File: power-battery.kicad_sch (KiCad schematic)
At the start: 6 parts, among them J2 S2B-PH-K-SLFSN, U5 MCP73831-2-OT

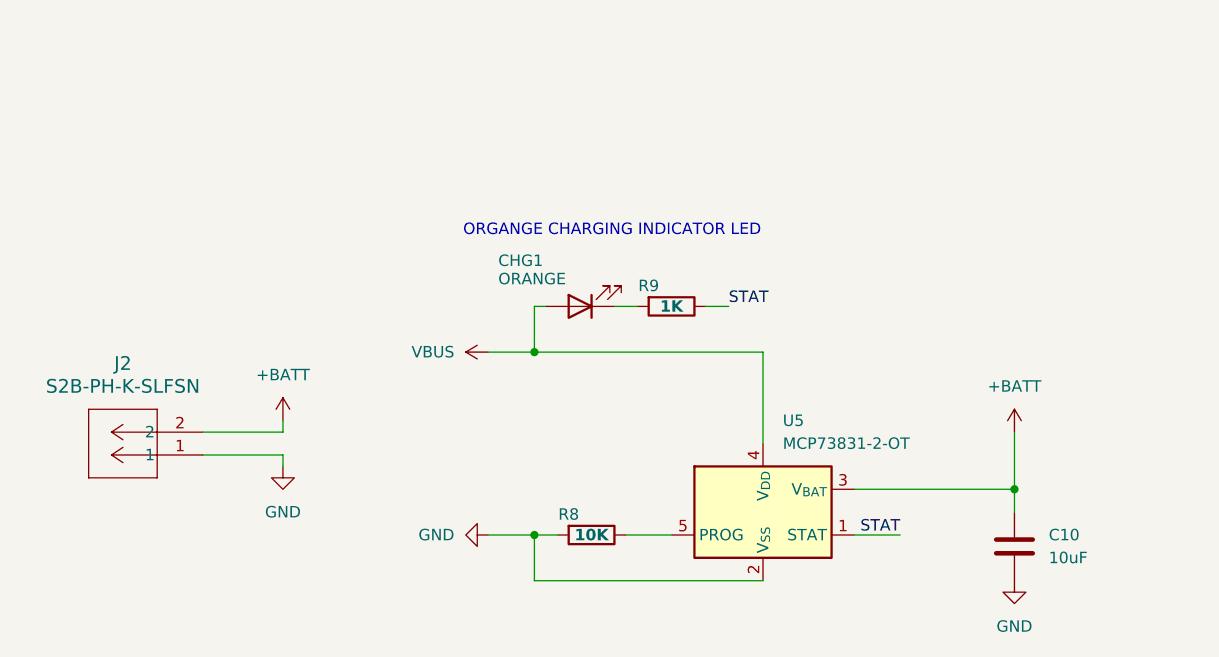
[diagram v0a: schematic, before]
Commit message: Adding symbols information
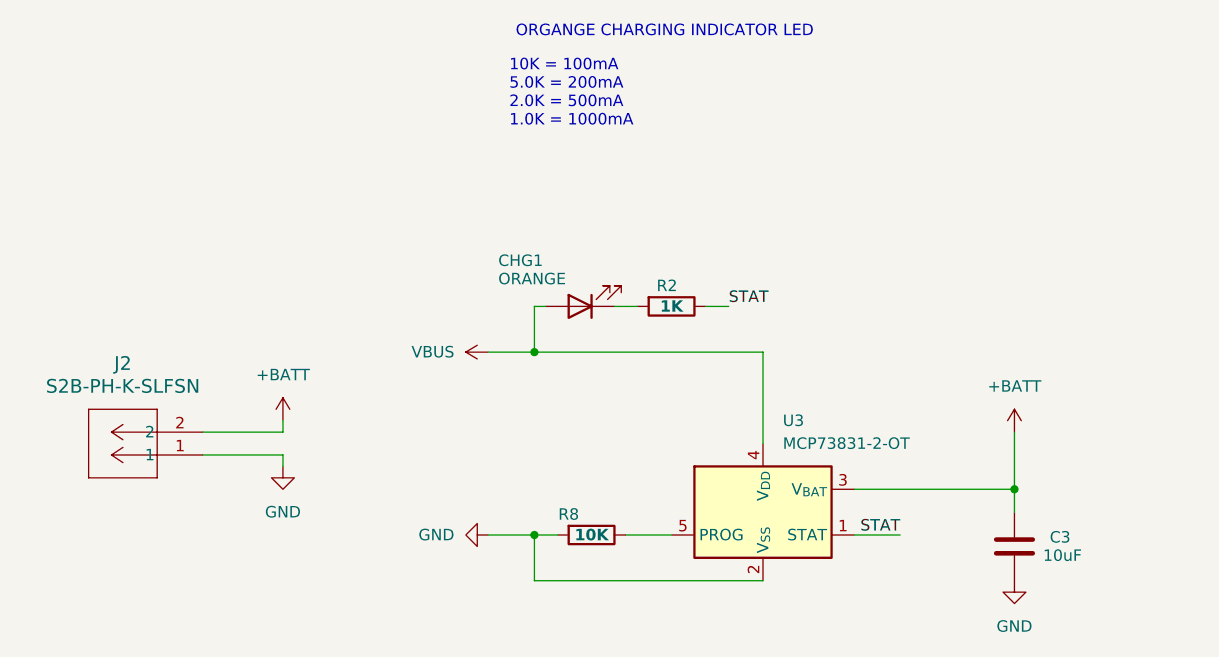
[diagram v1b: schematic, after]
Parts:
- removed C10: 10uF, symbol Device:C
- added C3: 10uF, Inductor_SMD:L_0805_2012Metric, symbol Device:C
- CHG1: footprint (none) -> LED_SMD:LED_0805_2012Metric; Mfr (none) -> Harvatek Corporation; Mfr P/N (none) -> B1701UD--20D000414U1930; Supplier_1 (none) -> Digikey; Supplier_1 P/N (none) -> 3147-B1701UD--20D000414U1930CT-ND; Supplier_1 Price @ Qty (none) -> 0.092; Supplier_1 Unit Price (none) -> 0.10
- R2: renamed from R9; footprint (none) -> Capacitor_SMD:C_0603_1608Metric; Mfr (none) -> Vishay Beyschlag/Draloric/BC Components; Mfr P/N (none) -> MCT06030C1001FP500; Supplier_1 (none) -> Digikey; Supplier_1 P/N (none) -> MCT0603-1.00K-CFCT-ND; Supplier_1 Price @ Qty (none) -> 0.02280; Supplier_1 Unit Price (none) -> 0.10
- U3: renamed from U5; Mfr (none) -> Microchip Technology; Mfr P/N (none) -> MCP73831T-2ATI/OT; Supplier_1 (none) -> Digikey; Supplier_1 P/N (none) -> MCP73831T-2AT|/OTCT-ND; Supplier_1 Price @ Qty (none) -> 0.6125; Supplier_1 Unit Price (none) -> 0.76
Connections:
- net +BATT: now also C3.1
- net GND: now also C3.2
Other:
- note added: "10K = 100mA 5.0K = 200mA 2.0K = 500mA 1.0K = 1000mA"
- company: (none) -> catbranchman
- title: (none) -> Power - Battery Charing

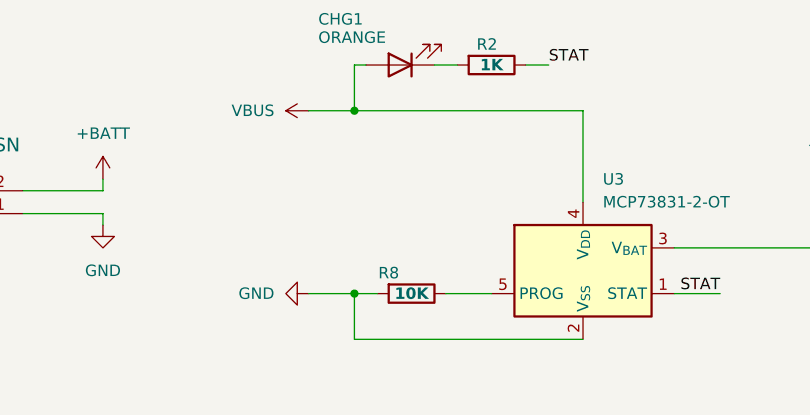
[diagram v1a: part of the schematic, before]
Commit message: Fixing footprint imports
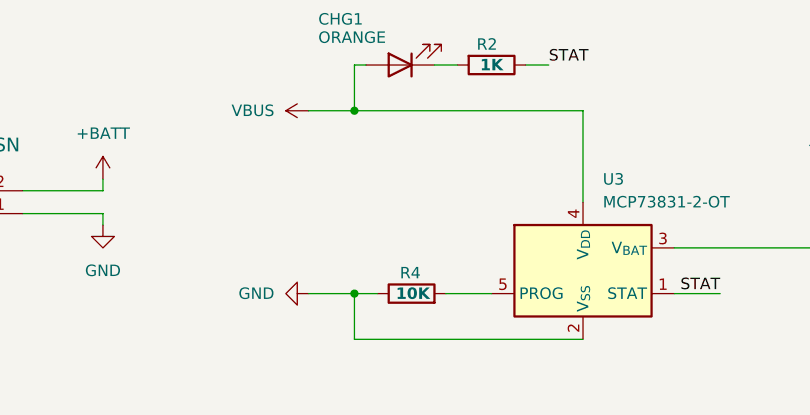
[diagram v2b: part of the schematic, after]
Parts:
- removed R8: 10K, symbol Device:R
- added R4: 10K, Resistor_SMD:R_0603_1608Metric, symbol Device:R
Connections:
- net GND: now also R4.1
- net at U3.5 (PROG): now also R4.2
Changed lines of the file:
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@@
-	)
-	(symbol
-		(lib_id "Device:R")
-		(at 146.05 109.22 270)
-		(unit 1)
-		(exclude_from_sim no)
-		(in_bom yes)
-		(on_board yes)
-		(dnp no)
-		(property "Reference" "R8"
-			(at 143.51 106.934 90)
-			(effects
-				(font
-					(size 1.27 1.27)
-				)
-			)
-		)
-		(property "Value" "10K"
-			(at 146.05 109.22 90)
-			(effects
-				(font
-					(size 1.27 1.27)
-					(thickness 0.254)
-					(bold yes)
-				)
-			)
-		)
-		(property "Footprint" ""
-			(at 146.05 107.442 90)
-			(effects
-				(font
-					(size 1.27 1.27)
-				)
-				(hide yes)
-			)
-		)
-		(property "Datasheet" "~"
-			(at 146.05 109.22 0)
-			(effects
-				(font
-					(size 1.27 1.27)
-				)
-				(hide yes)
-			)
-		)
-		(property "Description" "Resistor"
-			(at 146.05 109.22 0)
-			(effects
-				(font
-					(size 1.27 1.27)
-				)
-				(hide yes)
-			)
-		)
-		(pin "2"
-		)
-		(pin "1"
-		)
-		(instances
-			(project "roamer"
-				(path "/1c59de6a-87fe-4223-8898-4b0383164a31/8b882434-0721-40fe-a26c-3dd045b3f675"
-					(reference "R8")
-					(unit 1)
-				)
-			)
-		)
 	)
 	(symbol
@@
 					(unit 1)
 				)
+			)
+		)
+	)
+	(symbol
+		(lib_id "Device:R")
+		(at 146.05 109.22 90)
+		(unit 1)
+		(exclude_from_sim no)
+		(in_bom yes)
+		(on_board yes)
+		(dnp no)
+		(property "Reference" "R4"
+			(at 147.066 106.934 90)
+			(effects
+				(font
+					(size 1.27 1.27)
+				)
+				(justify left)
+			)
+		)
+		(property "Value" "10K"
+			(at 148.082 109.22 90)
+			(effects
+				(font
+					(size 1.27 1.27)
+					(thickness 0.254)
+					(bold yes)
+				)
+				(justify left)
+			)
+		)
+		(property "Footprint" "Resistor_SMD:R_0603_1608Metric"
+			(at 146.05 110.998 90)
+			(effects
+				(font
+					(size 1.27 1.27)
+				)
+				(hide yes)
+			)
+		)
+		(property "Datasheet" "https://www.seielect.com/catalog/sei-rncp.pdf"
+			(at 146.05 109.22 0)
+			(effects
+				(font
+					(size 1.27 1.27)
+				)
+				(hide yes)
+			)
+		)
+		(property "Description" "10 kOhms 1% 0.125W, 1/8W Chip Resistor 0603 (1608 Metric) Anti-Sulfur Thin Film"
+			(at 146.05 109.22 0)
+			(effects
+				(font
+					(size 1.27 1.27)
+				)
+				(hide yes)
+			)
+		)
+		(property "Mfr" "Stackpole Electronics Inc"
+			(at 146.05 109.22 0)
+			(effects
+				(font
+					(size 1.27 1.27)
+				)
+				(hide yes)
+			)
+		)
+		(property "Mfr P/N" "RNCP0603FTD10K0"
+			(at 146.05 109.22 0)
+			(effects
+				(font
+					(size 1.27 1.27)
+				)
+				(hide yes)
+			)
+		)
+		(property "Supplier_1" "Digikey"
+			(at 146.05 109.22 0)
+			(effects
+				(font
+					(size 1.27 1.27)
+				)
+				(hide yes)
+			)
+		)
+		(property "Supplier_1 P/N" "RNCP0603FTD10K0CT-ND"
+			(at 146.05 109.22 0)
+			(effects
+				(font
+					(size 1.27 1.27)
+				)
+				(hide yes)
+			)
+		)
+		(property "Supplier_1 Unit Price" "0.10"
+			(at 146.05 109.22 0)
+			(effects
+				(font
+					(size 1.27 1.27)
+				)
+				(hide yes)
+			)
+		)
+		(property "Supplier_1 Price @ Qty" "0.0170"
+			(at 146.05 109.22 0)
+			(effects
+				(font
+					(size 1.27 1.27)
+				)
+				(hide yes)
+			)
+		)
+		(property "Supplier_2" ""
+			(at 146.05 109.22 0)
+			(effects
+				(font
+					(size 1.27 1.27)
+				)
+				(hide yes)
+			)
+		)
+		(property "Supplier_2 P/N" ""
+			(at 146.05 109.22 0)
+			(effects
+				(font
+					(size 1.27 1.27)
+				)
+				(hide yes)
+			)
+		)
+		(property "Supplier_2 Unit Price" ""
+			(at 146.05 109.22 0)
+			(effects
+				(font
+					(size 1.27 1.27)
+				)
+				(hide yes)
+			)
+		)
+		(property "Supplier_2 Price @ Qty" ""
+			(at 146.05 109.22 0)
+			(effects
+				(font
+					(size 1.27 1.27)
+				)
+				(hide yes)
+			)
+		)
+		(pin "2"
+		)
+		(pin "1"
+		)
+		(instances
+			(project "roamer"
+				(path "/1c59de6a-87fe-4223-8898-4b0383164a31/8b882434-0721-40fe-a26c-3dd045b3f675"
+					(reference "R4")
+					(unit 1)
+				)

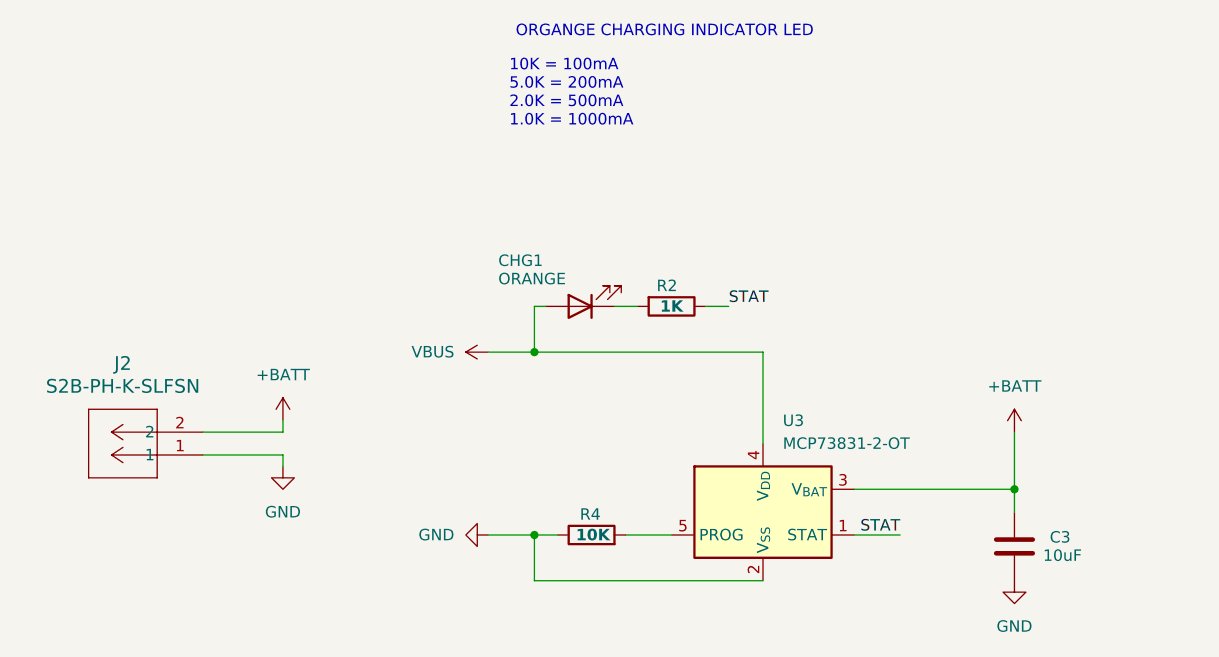
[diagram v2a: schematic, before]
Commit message: Adding more 0 ohm resistors and pullups for I2C lines
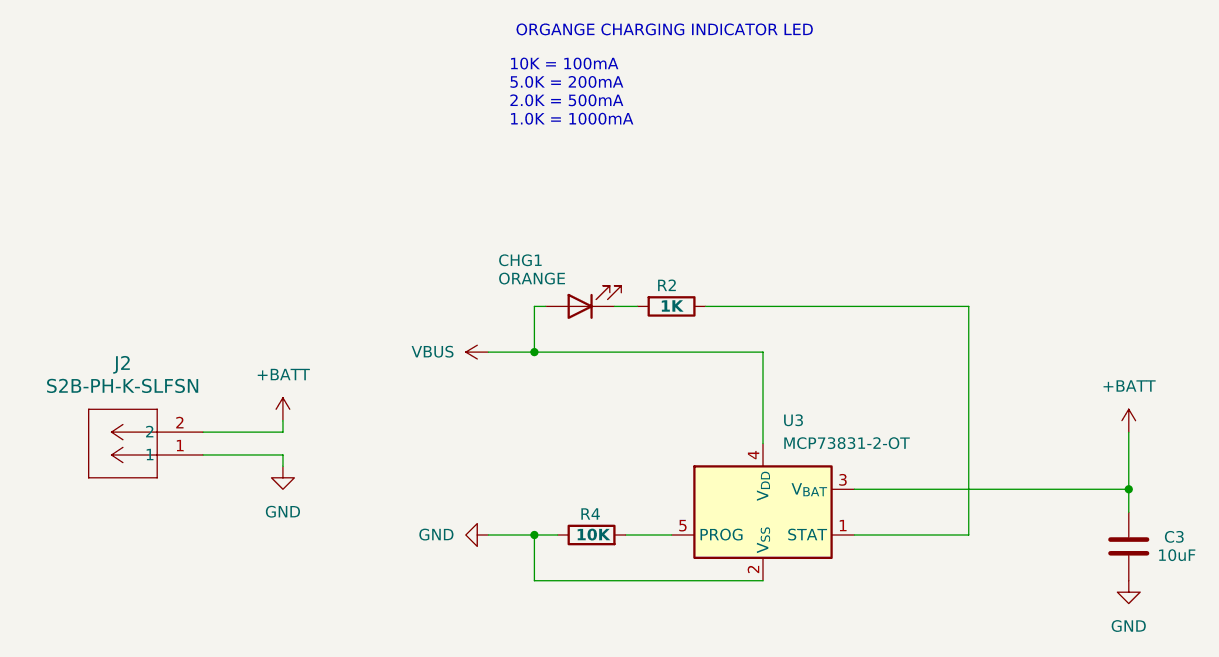
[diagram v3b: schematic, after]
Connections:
- net STAT: no longer names the net of R2.1, U3.1 (STAT)
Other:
- moved on the sheet: C3
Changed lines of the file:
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@@
 	)
 	(junction
-		(at 193.04 104.14)
+		(at 205.74 104.14)
 		(diameter 0)
 		(color 0 0 0 0)
@@
 	(wire
 		(pts
-			(xy 193.04 106.68) (xy 193.04 104.14)
+			(xy 205.74 106.68) (xy 205.74 104.14)
 		)
 		(stroke
@@
 	(wire
 		(pts
-			(xy 158.75 83.82) (xy 161.29 83.82)
+			(xy 158.75 83.82) (xy 187.96 83.82)
 		)
 		(stroke
@@
 	(wire
 		(pts
-			(xy 193.04 97.79) (xy 193.04 104.14)
-		)
-		(stroke
-			(width 0)
-			(type default)
-		)
-	)
-	(wire
-		(pts
-			(xy 175.26 104.14) (xy 193.04 104.14)
-		)
-		(stroke
-			(width 0)
-			(type default)
-		)
-	)
-	(wire
-		(pts
-			(xy 180.34 109.22) (xy 175.26 109.22)
+			(xy 205.74 97.79) (xy 205.74 104.14)
+		)
+		(stroke
+			(width 0)
+			(type default)
+		)
+	)
+	(wire
+		(pts
+			(xy 175.26 104.14) (xy 205.74 104.14)
+		)
+		(stroke
+			(width 0)
+			(type default)
+		)
+	)
+	(wire
+		(pts
+			(xy 175.26 109.22) (xy 187.96 109.22)
 		)
 		(stroke
@@
 		(pts
 			(xy 139.7 88.9) (xy 165.1 88.9)
+		)
+		(stroke
+			(width 0)
+			(type default)
+		)
+	)
+	(wire
+		(pts
+			(xy 187.96 109.22) (xy 187.96 83.82)
 		)
 		(stroke
@@
 				(size 1.27 1.27)
 			)
-		)
-	)
-	(label "STAT"
-		(at 180.34 109.22 180)
-		(fields_autoplaced yes)
-		(effects
-			(font
-				(size 1.27 1.27)
-			)
-			(justify right bottom)
-		)
-	)
-	(label "STAT"
-		(at 161.29 83.82 0)
-		(fields_autoplaced yes)
-		(effects
-			(font
-				(size 1.27 1.27)
-			)
-			(justify left bottom)
 		)
 	)
@@
 	(symbol
 		(lib_id "Device:C")
-		(at 193.04 110.49 0)
+		(at 205.74 110.49 0)
 		(unit 1)
 		(exclude_from_sim no)
@@
 		(dnp no)
 		(property "Reference" "C3"
-			(at 198.12 109.474 0)
+			(at 210.82 109.474 0)
 			(effects
 				(font
@@
 		)
 		(property "Value" "10uF"
-			(at 198.374 111.506 0)
+			(at 211.074 111.506 0)
 			(effects
 				(font
@@
 		)
 		(property "Footprint" "Inductor_SMD:L_0805_2012Metric"
-			(at 194.0052 114.3 0)
+			(at 206.7052 114.3 0)
 			(effects
 				(font
@@
 		)
 		(property "Datasheet" "https://mm.digikey.com/Volume0/opasdata/d220001/medias/docus/609/CL21A106K0QNNNE_Sp"
-			(at 193.04 110.49 0)
+			(at 205.74 110.49 0)
 			(effects
 				(font
@@
 		)
 		(property "Description" "10 uF 10% 16V Ceramic Capacitor X5R 0805 (2012 Metric)"
-			(at 193.04 110.49 0)
+			(at 205.74 110.49 0)
 			(effects
 				(font
@@
 		)
 		(property "Mfr" "Samsung Electro-Mechanics"
-			(at 193.04 110.49 0)
+			(at 205.74 110.49 0)
 			(effects
 				(font
@@
 		)
 		(property "Mfr P/N" "CL21A106KOQNNNE"
-			(at 193.04 110.49 0)
+			(at 205.74 110.49 0)
 			(effects
 				(font
@@
 		)
 		(property "Supplier_1" "Digikey"
-			(at 193.04 110.49 0)
+			(at 205.74 110.49 0)
 			(effects
 				(font
@@
 		)
 		(property "Supplier_1 P/N" "1276-1096-1-ND"
-			(at 193.04 110.49 0)
+			(at 205.74 110.49 0)
 			(effects
 				(font
@@
 		)
 		(property "Supplier_1 Unit Price" "0.10"
-			(at 193.04 110.49 0)
+			(at 205.74 110.49 0)
 			(effects
 				(font
@@
 		)
 		(property "Supplier_1 Price @ Qty" "0.03130"
-			(at 193.04 110.49 0)
+			(at 205.74 110.49 0)
 			(effects
 				(font
@@
 		)
 		(property "Supplier_2" ""
-			(at 193.04 110.49 0)
+			(at 205.74 110.49 0)
 			(effects
 				(font
@@
 		)
 		(property "Supplier_2 P/N" ""
-			(at 193.04 110.49 0)
+			(at 205.74 110.49 0)
 			(effects
 				(font
@@
 		)
 		(property "Supplier_2 Unit Price" ""
-			(at 193.04 110.49 0)
+			(at 205.74 110.49 0)
 			(effects
 				(font
@@
 		)
 		(property "Supplier_2 Price @ Qty" ""
-			(at 193.04 110.49 0)
+			(at 205.74 110.49 0)
 			(effects
 				(font
@@
 	(symbol
 		(lib_id "power:+BATT")
-		(at 193.04 97.79 0)
+		(at 205.74 97.79 0)
 		(unit 1)
 		(exclude_from_sim no)
@@
 		(fields_autoplaced yes)
 		(property "Reference" "#PWR031"
-			(at 193.04 101.6 0)
+			(at 205.74 101.6 0)
 			(effects
 				(font
@@
 		)
 		(property "Value" "+BATT"
-			(at 193.04 92.71 0)
+			(at 205.74 92.71 0)
 			(effects
 				(font
@@
 		)
 		(property "Footprint" ""
-			(at 193.04 97.79 0)
+			(at 205.74 97.79 0)
 			(effects
 				(font
@@
 		)
 		(property "Datasheet" ""
-			(at 193.04 97.79 0)
+			(at 205.74 97.79 0)
 			(effects
 				(font
@@
 		)
 		(property "Description" "Power symbol creates a global label with name \"+BATT\""
-			(at 193.04 97.79 0)
+			(at 205.74 97.79 0)
 			(effects
 				(font
@@
 	(symbol
 		(lib_id "power:GND")
-		(at 193.04 114.3 0)
+		(at 205.74 114.3 0)
 		(unit 1)
 		(exclude_from_sim no)
@@
 		(fields_autoplaced yes)
 		(property "Reference" "#PWR032"
-			(at 193.04 120.65 0)
+			(at 205.74 120.65 0)
 			(effects
 				(font
@@
 		)
 		(property "Value" "GND"
-			(at 193.04 119.38 0)
+			(at 205.74 119.38 0)
 			(effects
 				(font
@@
 		)
 		(property "Footprint" ""
-			(at 193.04 114.3 0)
+			(at 205.74 114.3 0)
 			(effects
 				(font
@@
 		)
 		(property "Datasheet" ""
-			(at 193.04 114.3 0)
+			(at 205.74 114.3 0)
 			(effects
 				(font
@@
 		)
 		(property "Description" "Power symbol creates a global label with name \"GND\" , ground"
-			(at 193.04 114.3 0)
-			(effects
-				(font
+			(at 205.74 114.3 0)
+			(effects
+				(font

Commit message: Working on layout
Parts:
- J2: value S2B-PH-K-SLFSN -> JSTPH; footprint CONN_S2B-PH-K-S_JST -> Connector_JST:JST_PH_S2B-PH-SM4-TB_1x02-1MP_P2.00mm_Horizontal; Mfr (none) -> JST Sales America Inc.; Mfr P/N (none) -> S2B-PH-SM4-TB; Supplier_1 (none) -> Digikey; Supplier_1 P/N (none) -> 455-S2B-PH-SM4-TBCT-ND; Supplier_1 Price @ Qty (none) -> 0.4143; Supplier_1 Unit Price (none) -> 0.58
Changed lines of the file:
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@@
 	(wire
 		(pts
-			(xy 111.76 97.79) (xy 102.87 97.79)
+			(xy 102.87 97.79) (xy 111.76 97.79)
 		)
 		(stroke
@@
 			)
 		)
-		(property "Value" "S2B-PH-K-SLFSN"
+		(property "Value" "JSTPH"
 			(at 93.98 92.71 0)
 			(effects
@@
 			)
 		)
-		(property "Footprint" "CONN_S2B-PH-K-S_JST"
+		(property "Footprint" "Connector_JST:JST_PH_S2B-PH-SM4-TB_1x02-1MP_P2.00mm_Horizontal"
 			(at 102.87 100.33 0)
 			(effects
@@
 			)
 		)
-		(property "Datasheet" "S2B-PH-K-SLFSN"
+		(property "Datasheet" "https://www.jst-mfg.com/product/pdf/eng/ePH.pdf"
 			(at 102.87 100.33 0)
 			(effects
@@
 			)
 		)
-		(property "Description" ""
-			(at 102.87 100.33 0)
-			(effects
+		(property "Description" "Connector Header Surface Mount, Right Angle 2 position 0.079\" (2.00mm)"
+			(at 102.87 100.33 0)
+			(effects
+				(font
+					(size 1.27 1.27)
+				)
+				(hide yes)
+			)
+		)
+		(property "Mfr" "JST Sales America Inc."
+			(at 102.87 100.33 0)
+			(effects
+				(font
+					(size 1.27 1.27)
+				)
+				(hide yes)
+			)
+		)
+		(property "Mfr P/N" "S2B-PH-SM4-TB"
+			(at 102.87 100.33 0)
+			(effects
+				(font
+					(size 1.27 1.27)
+				)
+				(hide yes)
+			)
+		)
+		(property "Supplier_1" "Digikey"
+			(at 102.87 100.33 0)
+			(effects
+				(font
+					(size 1.27 1.27)
+				)
+				(hide yes)
+			)
+		)
+		(property "Supplier_1 P/N" "455-S2B-PH-SM4-TBCT-ND"
+			(at 102.87 100.33 0)
+			(effects
+				(font
+					(size 1.27 1.27)
+				)
+				(hide yes)
+			)
+		)
+		(property "Supplier_1 Unit Price" "0.58"
+			(at 102.87 100.33 0)
+			(effects
+				(font
+					(size 1.27 1.27)
+				)
+				(hide yes)
+			)
+		)
+		(property "Supplier_1 Price @ Qty" "0.4143"
+			(at 102.87 100.33 0)
+			(effects
+				(font
+					(size 1.27 1.27)
+				)
+				(hide yes)
+			)
+		)
+		(property "Supplier_2" ""
+			(at 102.87 100.33 0)
+			(effects
+				(font
+					(size 1.27 1.27)
+				)
+				(hide yes)
+			)
+		)
+		(property "Supplier_2 P/N" ""
+			(at 102.87 100.33 0)
+			(effects
+				(font
+					(size 1.27 1.27)
+				)
+				(hide yes)
+			)
+		)
+		(property "Supplier_2 Unit Price" ""
+			(at 102.87 100.33 0)
+			(effects
+				(font
+					(size 1.27 1.27)
+				)
+				(hide yes)
+			)
+		)
+		(property "Supplier_2 Price @ Qty" ""
+			(at 102.87 100.33 0)
+			(effects
